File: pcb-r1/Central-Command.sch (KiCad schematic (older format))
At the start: 18 parts, among them P101 CONN_01X10, P102 CONN_01X10, P103 CONN_01X04, P104 CONN_01X02, P105 CONN_01X04, P106 CONN_01X02, U101 STM32F030C8, Y101 Crystal

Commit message: Updated the parts with further DigiKeyPN
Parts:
- C101, C104, C107: DigiKeyPN (none) -> 478-1395-1-ND
- C102, C103: DigiKeyPN (none) -> 1276-1829-1-ND
- C105, C108: DigiKeyPN (none) -> 311-1951-1-ND
- C106, C109: DigiKeyPN (none) -> 1276-2865-1-ND
- Y101: DigiKeyPN (none) -> 631-1100-ND
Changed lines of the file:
@@
 F 2 "Capacitors_SMD:C_0805" H 4038 900 30  0001 C CNN
 F 3 "" H 4000 1050 60  0000 C CNN
+F 4 "478-1395-1-ND" H 4000 1050 60  0001 C CNN "DigiKeyPN"
 	1    4000 1050
 	1    0    0    -1
@@
 F 4 "http://parts.io/detail/343558/FOXSLF%2F080-20" H 4650 1750 60  0001 C CNN "Link"
 F 5 "FOXSLF/080-20" H 4650 1750 60  0001 C CNN "MPN"
+F 6 "631-1100-ND" H 4650 1750 60  0001 C CNN "DigiKeyPN"
 	1    4650 1750
 	0    1    1    0
@@
 F 2 "Capacitors_SMD:C_0805" H 5288 1850 30  0001 C CNN
 F 3 "" H 5250 2000 60  0000 C CNN
+F 4 "1276-1829-1-ND" H 5250 2000 60  0001 C CNN "DigiKeyPN"
 	1    5250 2000
 	0    -1   -1   0
@@
 F 2 "Capacitors_SMD:C_0805" H 5288 1400 30  0001 C CNN
 F 3 "" H 5250 1550 60  0000 C CNN
+F 4 "1276-1829-1-ND" H 5250 1550 60  0001 C CNN "DigiKeyPN"
 	1    5250 1550
 	0    -1   -1   0
@@
 F 2 "Capacitors_SMD:C_0805" H 6988 1050 30  0001 C CNN
 F 3 "" H 6950 1200 60  0000 C CNN
+F 4 "478-1395-1-ND" H 6950 1200 60  0001 C CNN "DigiKeyPN"
 	1    6950 1200
 	-1   0    0    1
@@
 F 2 "Capacitors_SMD:C_1206" H 7438 1050 30  0001 C CNN
 F 3 "" H 7400 1200 60  0000 C CNN
+F 4 "311-1951-1-ND" H 7400 1200 60  0001 C CNN "DigiKeyPN"
 	1    7400 1200
 	-1   0    0    1
@@
 F 2 "Capacitors_SMD:C_1206" H 7838 1050 30  0001 C CNN
 F 3 "" H 7800 1200 60  0000 C CNN
+F 4 "1276-2865-1-ND" H 7800 1200 60  0001 C CNN "DigiKeyPN"
 	1    7800 1200
 	-1   0    0    1
@@
 F 2 "Capacitors_SMD:C_0805" H 8538 1050 30  0001 C CNN
 F 3 "" H 8500 1200 60  0000 C CNN
+F 4 "478-1395-1-ND" H 8500 1200 60  0001 C CNN "DigiKeyPN"
 	1    8500 1200
 	-1   0    0    1
@@
 F 2 "Capacitors_SMD:C_1206" H 8988 1050 30  0001 C CNN
 F 3 "" H 8950 1200 60  0000 C CNN
+F 4 "311-1951-1-ND" H 8950 1200 60  0001 C CNN "DigiKeyPN"
 	1    8950 1200
 	-1   0    0    1
@@
 F 2 "Capacitors_SMD:C_1206" H 9388 1050 30  0001 C CNN
 F 3 "" H 9350 1200 60  0000 C CNN
+F 4 "1276-2865-1-ND" H 9350 1200 60  0001 C CNN "DigiKeyPN"
 	1    9350 1200
 	-1   0    0    1

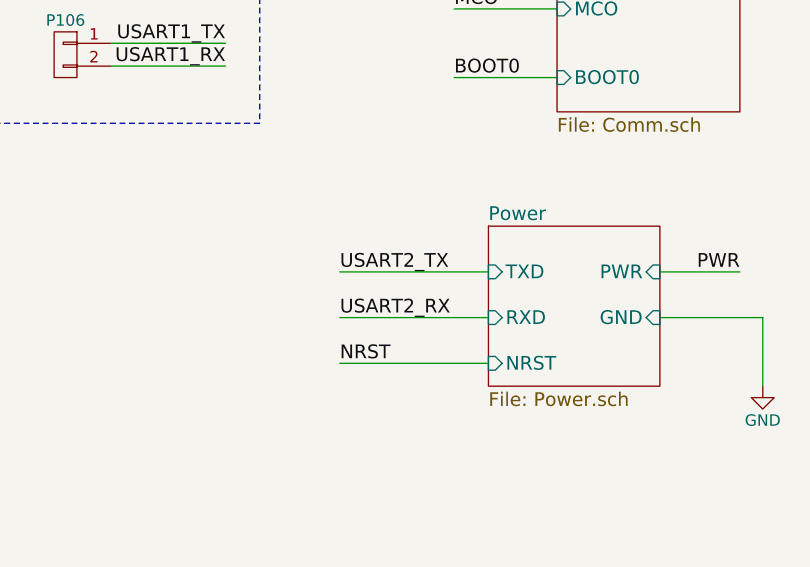
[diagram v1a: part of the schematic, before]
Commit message: Made the correction to the Tx Rx on the schematic and added a comment regarding the Ferrite Bead
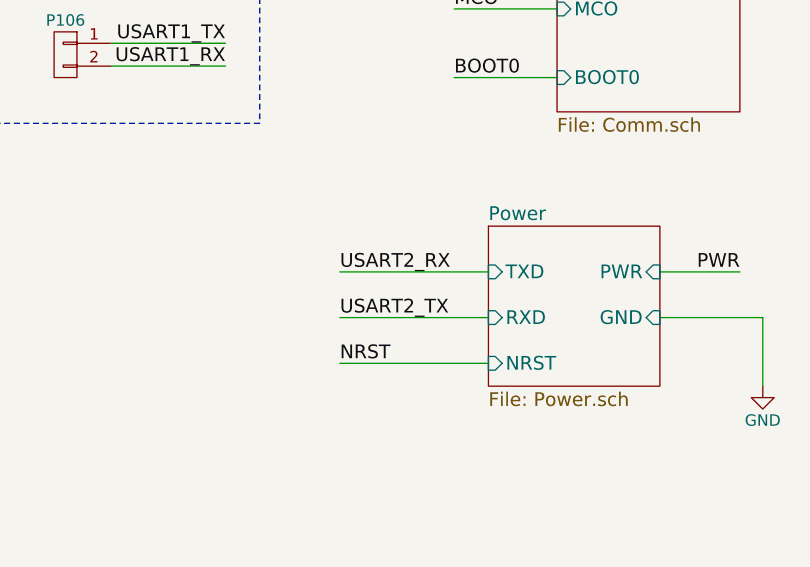
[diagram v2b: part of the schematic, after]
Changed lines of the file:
@@
 Text Notes 5750 5550 2    60   ~ 0
 Sensor I2C Header
+Text Label 7600 5850 0    60   ~ 0
+USART2_TX
 Text Label 7600 5650 0    60   ~ 0
-USART2_TX
-Text Label 7600 5850 0    60   ~ 0
 USART2_RX
 $Comp
